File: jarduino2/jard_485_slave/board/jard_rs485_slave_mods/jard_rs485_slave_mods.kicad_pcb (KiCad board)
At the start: 2 copper layers, 90 x 85 mm, 38 parts, among them J1 NETWORK IN, J2 NETWORK OUT, J3 LED, J4 LED, J5 Debit, J6 Niveau, J7 Electrovanne 12V, Q1 BPC_2N2222A, Q2 P03P4L-04, U1 BPC_Mod485, U2 BPC_DHT22, U3 LM358

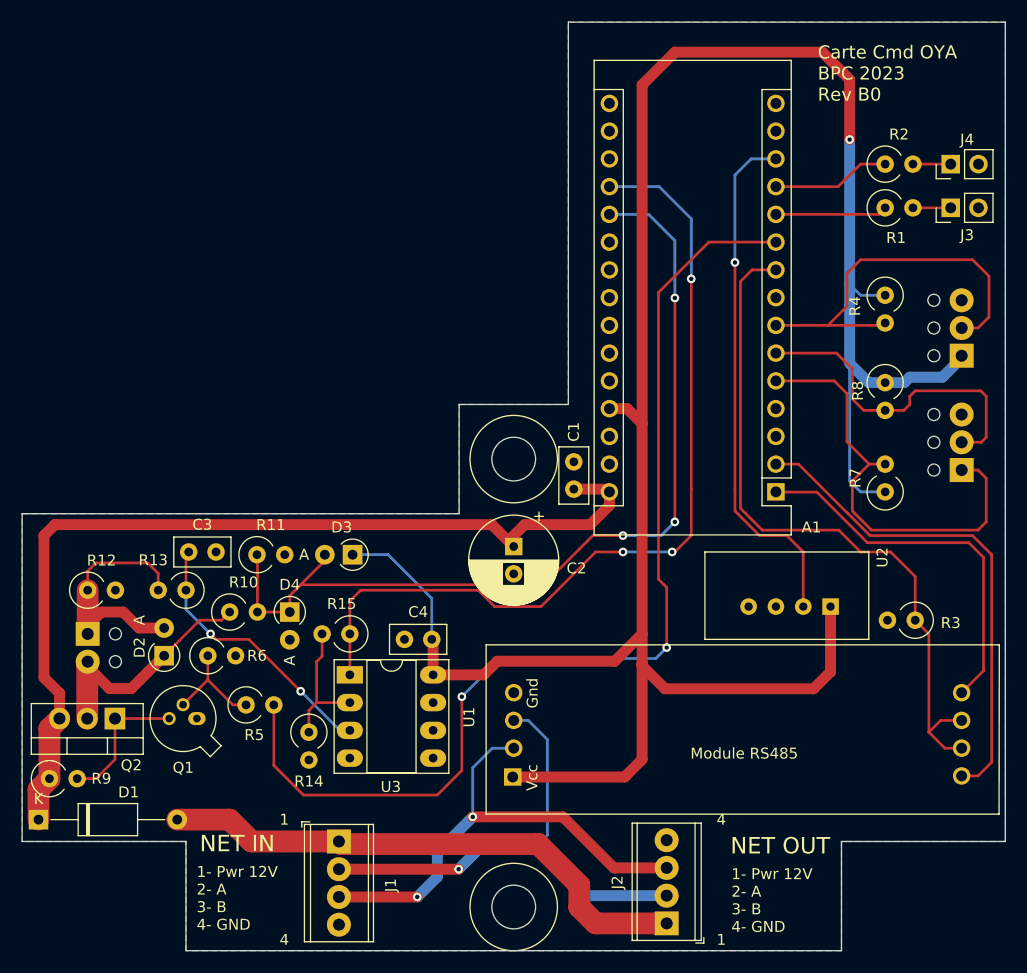
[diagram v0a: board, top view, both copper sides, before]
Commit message: Passage à Kicad V7.0 Ajout de switches pour l'adresse de l'esclave
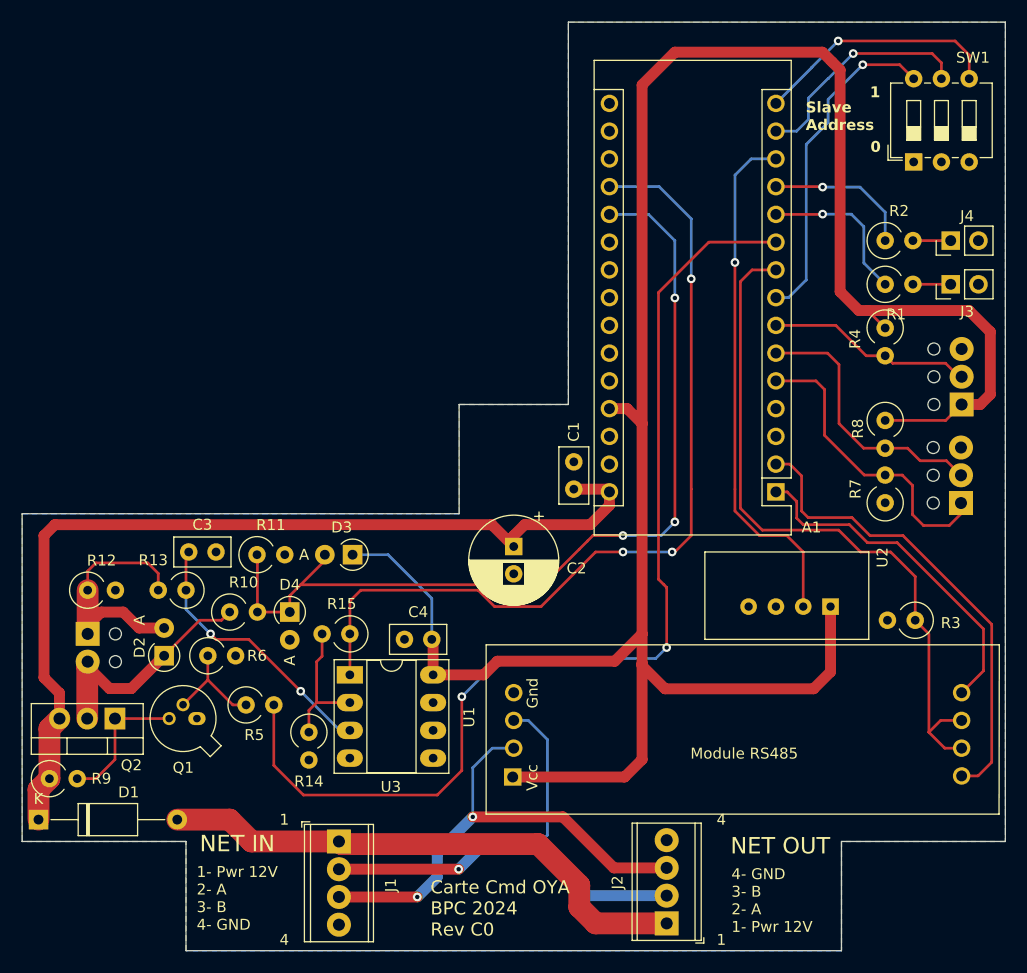
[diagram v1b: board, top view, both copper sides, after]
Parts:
- removed REF** (x2): BPC_Trou4mm_Fixation, bpc:BPC_Trou4mm_Fixation
- added SW1: Address, Button_Switch_THT:SW_DIP_SPSTx03_Slide_6.7x9.18mm_W7.62mm_P2.54mm_LowProfile, F.Cu at (182.6, 57.8)
- moved J3 7.00 mm to (186.0, 69.0)
- moved J4 7.00 mm to (186.0, 65.0)
- moved R1 7.00 mm to (180.0, 69.0)
- moved R2 7.00 mm to (180.0, 65.0)
- moved J5 4.46 mm to (187.0, 80.0)
- moved R8 3.46 mm to (180.0, 81.5)
- moved J6 3.02 mm to (186.9, 89.0)
- moved R4 3.00 mm to (180.0, 73.0)
- moved R7 1.00 mm to (180.0, 89.0)
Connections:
- A1 pad 16: Net-(A1-Pad16) -> unconnected-(A1-D13-Pad16)
- A1 pad 17: Net-(A1-Pad17) -> unconnected-(A1-3V3-Pad17)
- A1 pad 18: Net-(A1-Pad18) -> unconnected-(A1-AREF-Pad18)
- A1 pad 21: Net-(A1-Pad21) -> unconnected-(A1-A2-Pad21)
- A1 pad 22: Net-(A1-Pad22) -> unconnected-(A1-A3-Pad22)
- A1 pad 23: Net-(A1-Pad23) -> unconnected-(A1-A4-Pad23)
- A1 pad 24: Net-(A1-Pad24) -> unconnected-(A1-A5-Pad24)
- A1 pad 25: Net-(A1-Pad25) -> unconnected-(A1-A6-Pad25)
- A1 pad 26: Net-(A1-Pad26) -> unconnected-(A1-A7-Pad26)
- A1 pad 28: Net-(A1-Pad28) -> unconnected-(A1-~{RESET}-Pad28)
- A1 pad 3: Net-(A1-Pad3) -> unconnected-(A1-~{RESET}-Pad3)
- U2 pad 3: Net-(U2-Pad3) -> unconnected-(U2-NC-Pad3)
- U3 pad 7: Net-(U3-Pad7) -> unconnected-(U3-Pad7)
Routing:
- net Net-(A1-D5): track 0.00 -> 30.5 mm, vias 0 -> 1
- net Net-(A1-D12): track 0.00 -> 22.8 mm, vias 0 -> 1
- net Net-(A1-D11): track 0.00 -> 21.0 mm, vias 0 -> 1
- net FLOW_IN: track 36.4 -> 18.9 mm
- net IN_LVL_LOW: track 40.5 -> 27.9 mm
- net IN_LVL_HIGH: track 30.6 -> 24.7 mm
- net LED1: track 10.2 -> 14.6 mm, vias 0 -> 1
- net Vcc: track 217.1 -> 213.9 mm, vias 1 -> 0
- net TX: track 34.7 -> 31.8 mm
- net LED2: track 10.9 -> 13.6 mm, vias 0 -> 1
- net RX: track 45.5 -> 43.6 mm
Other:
- net class Default removed
- board text added: "0"
- board text added: "4- GND 3- B 2- A 1- Pwr 12V"
- board text added: "Carte Cmd OYA BPC 2024 Rev C0"
- board text added: "Slave Address"
- board text removed: "Carte Cmd OYA BPC 2023 Rev B0"
